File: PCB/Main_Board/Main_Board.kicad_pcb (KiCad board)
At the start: 2 copper layers, 68.2 x 58.9 mm, 57 parts, among them IC1 74LV1T34GVH, J1 USB_B_Micro, J2 Screw_Terminal_01x02, J3 SJ1-3523N, J4 SJ1-3523N, J5 Screw_Terminal_01x04, J6 Screw_Terminal_01x06, Q1 MBT3904DW1, SW1 SW_SPDT, SW2 EN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

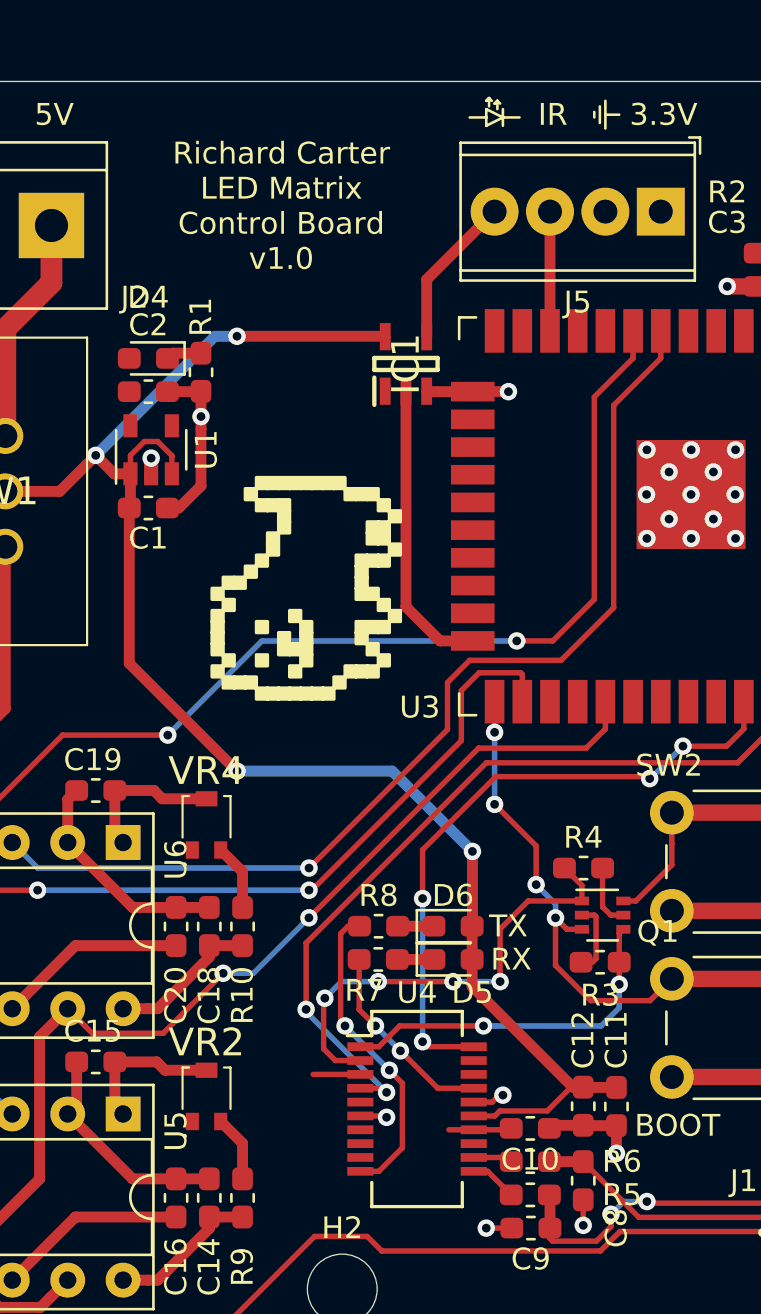
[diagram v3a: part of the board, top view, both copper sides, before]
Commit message: Move references and change renders
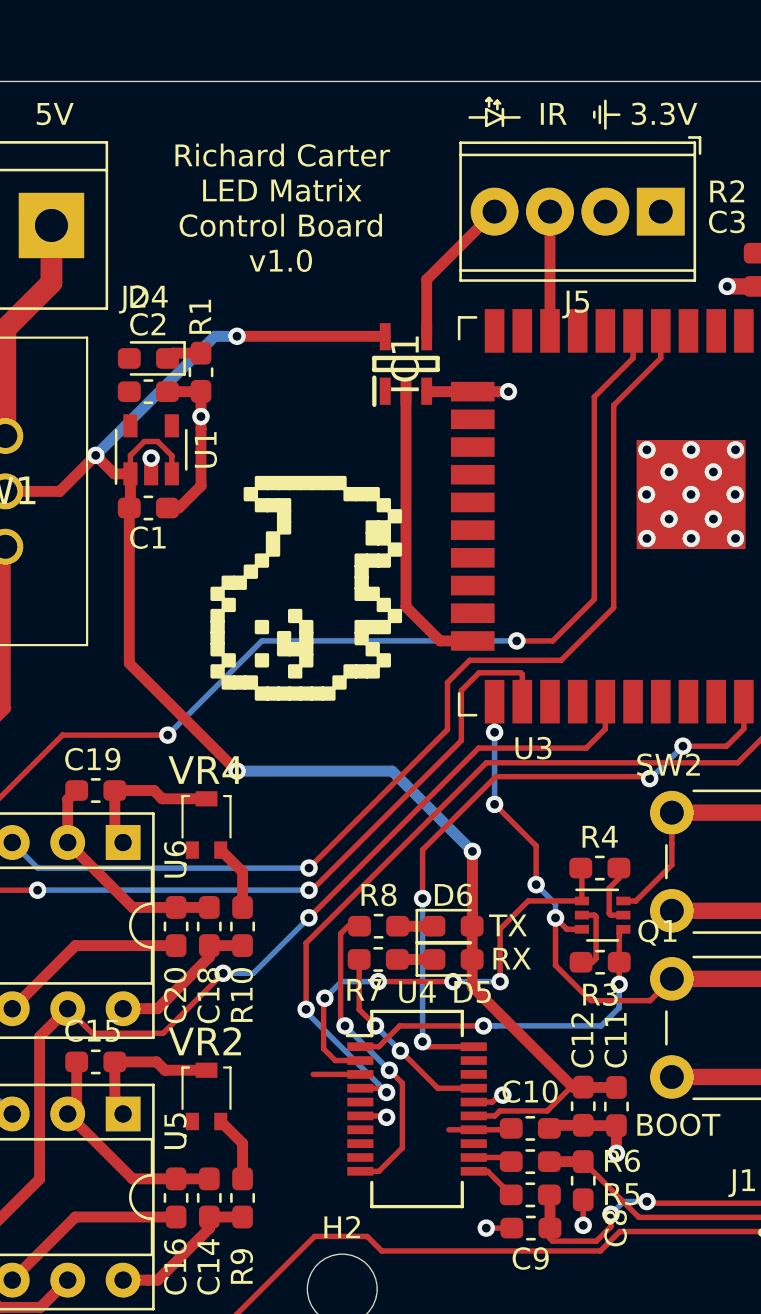
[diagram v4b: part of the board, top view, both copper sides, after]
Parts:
- moved R4 0.75 mm to (70.1, 55.9)
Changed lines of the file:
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@@
     (thickness 1.6)
     (drawings 68)
-    (tracks 420)
+    (tracks 422)
     (zones 0)
     (modules 57)
@@
   )
   (setup
-    (last_trace_width 0.5)
+    (last_trace_width 0.25)
     (user_trace_width 0.5)
     (user_trace_width 0.75)
@@
     (tags "Single 2.4 GHz Wi-Fi and Bluetooth combo  chip")
     (attr smd)
-    (fp_text reference U3 (at 8.763 11.684) (layer F.SilkS)
+    (fp_text reference U3 (at 10.668 6.477) (layer F.SilkS)
       (effects (font (size 1 1) (thickness 0.15)))
     )
@@
   )
   (module Resistor_SMD:R_0603_1608Metric_Pad1.05x0.95mm_HandSolder (layer F.Cu)
-    (at 69.356 55.88 180)
+    (at 70.104 55.88 180)
     (descr "Resistor SMD 0603 (1608 Metric), square (rectangular) end terminal, IPC_7351 nominal with elongated pad for handsoldering. (Body size source: http://www.tortai-tech.com/upload/download/2011102023233369053.pdf), generated with kicad-footprint-generator")
     (tags "resistor handsolder")
@@
     (tags "capacitor handsolder")
     (attr smd)
-    (fp_text reference C10 (at 0 -1.43) (layer F.SilkS)
+    (fp_text reference C10 (at 0 1.651) (layer F.SilkS)
       (effects (font (size 1 1) (thickness 0.15)))
     )
@@
     (arrow2b (pts (xy 24.765 80.391) (xy 25.891504 79.804579)))
   )
-  (gr_text "Richard Carter\nLED Matrix\nControl Board\nv1.0" (at 55.499 25.527) (layer F.SilkS)
+  (gr_text "Richard Carter\nLED Matrix\nControl Board\nv1.0" (at 55.499 25.654) (layer F.SilkS)
     (effects (font (size 1 1) (thickness 0.2)))
   )
@@
   (segment (start 69.931001 58.114001) (end 69.856 58.039) (width 0.25) (layer F.Cu) (net 27))
   (segment (start 70.606 58.039) (end 71.181 58.039) (width 0.25) (layer F.Cu) (net 28))
-  (segment (start 70.231 57.664) (end 70.606 58.039) (width 0.25) (layer F.Cu) (net 28))
-  (segment (start 70.231 55.88) (end 70.231 57.664) (width 0.25) (layer F.Cu) (net 28))
-  (segment (start 69.281 56.68) (end 68.481 55.88) (width 0.25) (layer F.Cu) (net 29))
-  (segment (start 69.281 57.389) (end 69.281 56.68) (width 0.25) (layer F.Cu) (net 29))
+  (segment (start 70.530999 57.963999) (end 70.606 58.039) (width 0.25) (layer F.Cu) (net 28))
+  (segment (start 70.530999 56.803001) (end 70.530999 57.963999) (width 0.25) (layer F.Cu) (net 28))
+  (segment (start 70.979 56.355) (end 70.530999 56.803001) (width 0.25) (layer F.Cu) (net 28))
+  (segment (start 70.979 55.88) (end 70.979 56.355) (width 0.25) (layer F.Cu) (net 28))
   (via (at 65.532 61.087) (size 0.8) (drill 0.4) (layers F.Cu B.Cu) (net 29))
   (segment (start 66.817 57.389) (end 69.281 57.389) (width 0.25) (layer F.Cu) (net 29))
@@
   (segment (start 58.25599 61.087) (end 59.944 61.087) (width 0.25) (layer B.Cu) (net 29))
   (segment (start 57.49399 61.849) (end 58.25599 61.087) (width 0.25) (layer B.Cu) (net 29))
+  (segment (start 69.281 55.932) (end 69.229 55.88) (width 0.25) (layer F.Cu) (net 29))
+  (segment (start 69.281 57.389) (end 69.281 55.932) (width 0.25) (layer F.Cu) (net 29))
   (segment (start 64.9605 69.7865) (end 66.04 70.866) (width 0.25) (layer F.Cu) (net 30))
   (segment (start 64.322 69.7865) (end 64.9605 69.7865) (width 0.25) (layer F.Cu) (net 30))

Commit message: Fix plane routing and change dog icon
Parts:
- U2: footprint Artwork:dog_logo -> Artwork:dog_2_small
- moved U2 5.39 mm to (61.3, 40.4)

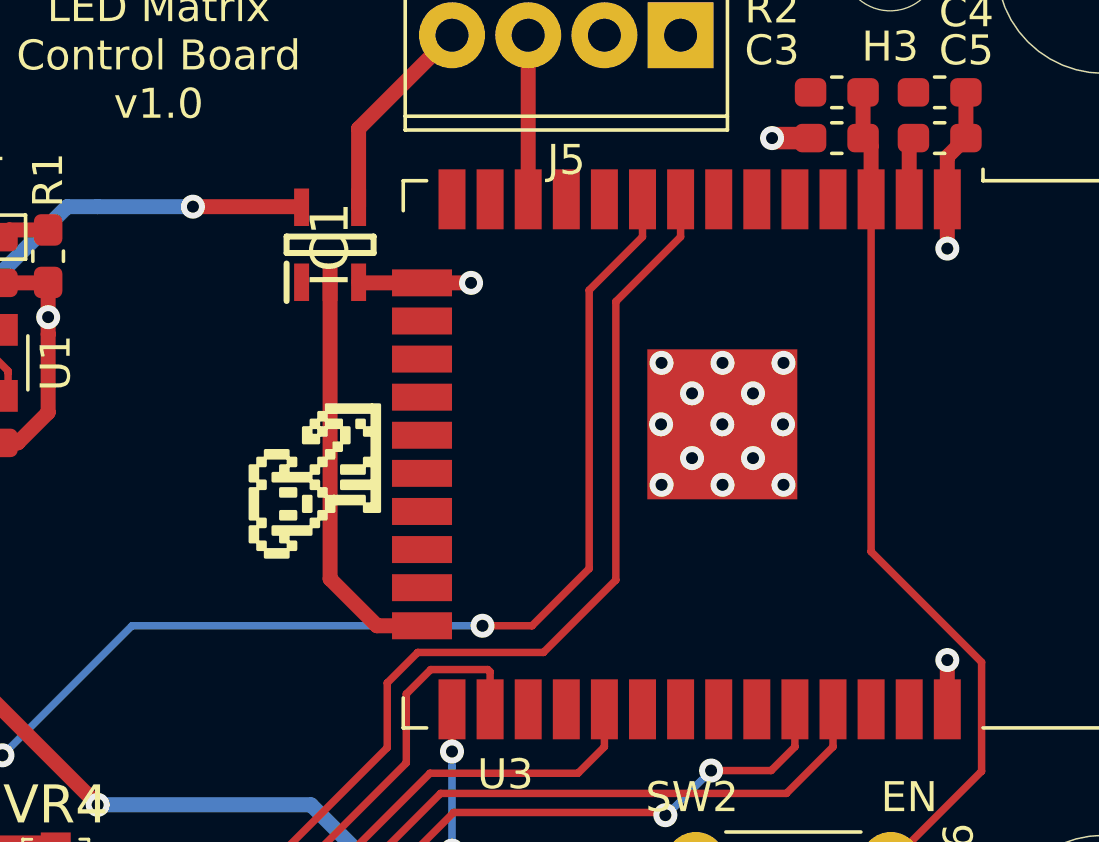
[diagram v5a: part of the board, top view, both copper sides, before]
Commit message: Add new art and JLC order number under ESP32-WROOM-32
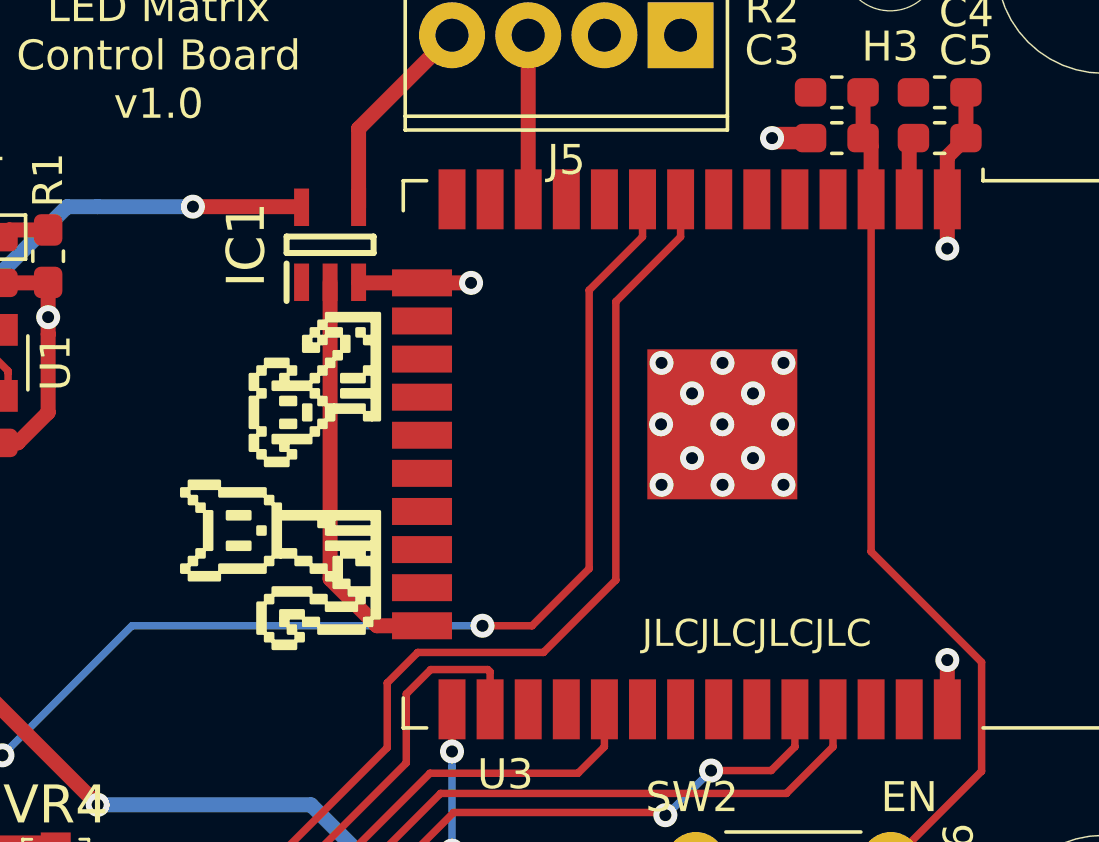
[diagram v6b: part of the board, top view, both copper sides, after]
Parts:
- added ART2: Artwork, Artwork:cat_small_mirrored, F.Cu at (60.6, 43.4)
- moved ART1 3.05 mm to (61.3, 37.3)
- renumbered U2 to ART1
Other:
- board text added: "JLCJLCJLCJLC"
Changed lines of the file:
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@@
   (general
     (thickness 1.6)
-    (drawings 68)
+    (drawings 69)
     (tracks 423)
     (zones 0)
-    (modules 57)
+    (modules 58)
     (nets 84)
   )
@@
     (38 B.Mask user)
     (39 F.Mask user)
-    (40 Dwgs.User user)
+    (40 Dwgs.User user hide)
     (41 Cmts.User user)
     (42 Eco1.User user)
@@
   )
   (setup
-    (last_trace_width 0.5)
+    (last_trace_width 0.25)
     (user_trace_width 0.5)
     (user_trace_width 0.75)
@@
     (add_net "Net-(VR4-Pad1)")
   )
+  (module Artwork:cat_small_mirrored (layer F.Cu)
+    (at 60.579 43.434 90)
+    (fp_text reference ART2 (at 0 -5.334 90) (layer Cmts.User)
+      (effects (font (size 1 1) (thickness 0.15)))
+    )
+    (fp_text value Artwork (at 0.254 3.302 90) (layer F.Fab)
+      (effects (font (size 1 1) (thickness 0.15)))
+    )
+    (fp_poly (pts (xy 2.286 -4.064) (xy 2.54 -4.064) (xy 2.54 -4.318) (xy 2.286 -4.318)) (layer F.SilkS) (width 0.1))
+    (fp_poly (pts (xy 2.032 -3.81) (xy 2.286 -3.81) (xy 2.286 -4.064) (xy 2.032 -4.064)) (layer F.SilkS) (width 0.1))
+    (fp_poly (pts (xy 1.778 -3.556) (xy 2.032 -3.556) (xy 2.032 -3.81) (xy 1.778 -3.81)) (layer F.SilkS) (width 0.1))
+    (fp_poly (pts (xy 2.54 -3.048) (xy 2.794 -3.048) (xy 2.794 -4.064) (xy 2.54 -4.064)) (layer F.SilkS) (width 0.1))
+    (fp_poly (pts (xy 0.508 -3.302) (xy 1.778 -3.302) (xy 1.778 -3.556) (xy 0.508 -3.556)) (layer F.SilkS) (width 0.1))
+    (fp_poly (pts (xy 0.254 -3.556) (xy 0.508 -3.556) (xy 0.508 -3.81) (xy 0.254 -3.81)) (layer F.SilkS) (width 0.1))
+    (fp_poly (pts (xy 0 -3.81) (xy 0.254 -3.81) (xy 0.254 -4.064) (xy 0 -4.064)) (layer F.SilkS) (width 0.1))
+    (fp_poly (pts (xy -0.254 -4.064) (xy 0 -4.064) (xy 0 -4.318) (xy -0.254 -4.318)) (layer F.SilkS) (width 0.1))
+    (fp_poly (pts (xy -0.508 -3.048) (xy -0.254 -3.048) (xy -0.254 -4.064) (xy -0.508 -4.064)) (layer F.SilkS) (width 0.1))
+    (fp_poly (pts (xy 1.524 -2.032) (xy 1.778 -2.032) (xy 1.778 -2.794) (xy 1.524 -2.794)) (layer F.SilkS) (width 0.1))
+    (fp_poly (pts (xy 0.508 -2.032) (xy 0.762 -2.032) (xy 0.762 -2.794) (xy 0.508 -2.794)) (layer F.SilkS) (width 0.1))
+    (fp_poly (pts (xy 2.286 -1.524) (xy 2.54 -1.524) (xy 2.54 -3.048) (xy 2.286 -3.048)) (layer F.SilkS) (width 0.1))
+    (fp_poly (pts (xy -0.254 -1.524) (xy 0 -1.524) (xy 0 -3.048) (xy -0.254 -3.048)) (layer F.SilkS) (width 0.1))
+    (fp_poly (pts (xy 2.032 -1.27) (xy 2.286 -1.27) (xy 2.286 -1.524) (xy 2.032 -1.524)) (layer F.SilkS) (width 0.1))
+    (fp_poly (pts (xy 0 -1.27) (xy 0.254 -1.27) (xy 0.254 -1.524) (xy 0 -1.524)) (layer F.SilkS) (width 0.1))
+    (fp_poly (pts (xy 0.254 -1.016) (xy 2.032 -1.016) (xy 2.032 -1.27) (xy 0.254 -1.27)) (layer F.SilkS) (width 0.1))
+    (fp_poly (pts (xy 0.254 -0.508) (xy 0.508 -0.508) (xy 0.508 -1.016) (xy 0.254 -1.016)) (layer F.SilkS) (width 0.1))
+    (fp_poly (pts (xy 0 0) (xy 0.254 0) (xy 0.254 -0.508) (xy 0 -0.508)) (layer F.SilkS) (width 0.1))
+    (fp_poly (pts (xy -0.254 0.508) (xy 0 0.508) (xy 0 0) (xy -0.254 0)) (layer F.SilkS) (width 0.1))
+    (fp_poly (pts (xy -0.508 0.762) (xy -0.254 0.762) (xy -0.254 0.508) (xy -0.508 0.508)) (layer F.SilkS) (width 0.1))
+    (fp_poly (pts (xy -0.762 1.016) (xy 0.254 1.016) (xy 0.254 0.762) (xy -0.762 0.762)) (layer F.SilkS) (width 0.1))
+    (fp_poly (pts (xy 0.254 1.778) (xy 0.508 1.778) (xy 0.508 1.016) (xy 0.254 1.016)) (layer F.SilkS) (width 0.1))
+    (fp_poly (pts (xy 0 2.032) (xy 0.254 2.032) (xy 0.254 1.524) (xy 0 1.524)) (layer F.SilkS) (width 0.1))
+    (fp_poly (pts (xy 0.508 2.032) (xy 0.762 2.032) (xy 0.762 0.508) (xy 0.508 0.508)) (layer F.SilkS) (width 0.1))
+    (fp_poly (pts (xy -0.762 1.27) (xy -0.508 1.27) (xy -0.508 1.016) (xy -0.762 1.016)) (layer F.SilkS) (width 0.1))
+    (fp_poly (pts (xy -1.016 2.032) (xy -0.762 2.032) (xy -0.762 1.27) (xy -1.016 1.27)) (layer F.SilkS) (width 0.1))
+    (fp_poly (pts (xy -1.27 1.778) (xy -1.016 1.778) (xy -1.016 1.524) (xy -1.27 1.524)) (layer F.SilkS) (width 0.1))
+    (fp_poly (pts (xy -1.524 1.524) (xy -1.27 1.524) (xy -1.27 0.508) (xy -1.524 0.508)) (layer F.SilkS) (width 0.1))
+    (fp_poly (pts (xy -1.27 0.508) (xy -1.016 0.508) (xy -1.016 0) (xy -1.27 0)) (layer F.SilkS) (width 0.1))
+    (fp_poly (pts (xy -2.032 0.254) (xy -1.778 0.254) (xy -1.778 -0.254) (xy -2.032 -0.254)) (layer F.SilkS) (width 0.1))
+    (fp_poly (pts (xy -2.286 1.778) (xy -2.032 1.778) (xy -2.032 0.254) (xy -2.286 0.254)) (layer F.SilkS) (width 0.1))
+    (fp_poly (pts (xy -2.032 2.032) (xy -1.778 2.032) (xy -1.778 1.778) (xy -2.032 1.778)) (layer F.SilkS) (width 0.1))
+    (fp_poly (pts (xy -1.778 -0.254) (xy -1.524 -0.254) (xy -1.524 -1.016) (xy -1.778 -1.016)) (layer F.SilkS) (width 0.1))
+    (fp_poly (pts (xy -2.032 -0.762) (xy -1.778 -0.762) (xy -1.778 -1.016) (xy -2.032 -1.016)) (layer F.SilkS) (width 0.1))
+    (fp_poly (pts (xy -2.286 -0.508) (xy -2.032 -0.508) (xy -2.032 -0.762) (xy -2.286 -0.762)) (layer F.SilkS) (width 0.1))
+    (fp_poly (pts (xy -2.54 -0.254) (xy -2.286 -0.254) (xy -2.286 -0.508) (xy -2.54 -0.508)) (layer F.SilkS) (width 0.1))
+    (fp_poly (pts (xy -2.794 -0.508) (xy -2.54 -0.508) (xy -2.54 -1.27) (xy -2.794 -1.27)) (layer F.SilkS) (width 0.1))
+    (fp_poly (pts (xy -2.54 -1.27) (xy -2.286 -1.27) (xy -2.286 -1.524) (xy -2.54 -1.524)) (layer F.SilkS) (width 0.1))
+    (fp_poly (pts (xy -2.286 -1.524) (xy -1.27 -1.524) (xy -1.27 -1.778) (xy -2.286 -1.778)) (layer F.SilkS) (width 0.1))
+    (fp_poly (pts (xy -1.27 -1.27) (xy -1.016 -1.27) (xy -1.016 -1.524) (xy -1.27 -1.524)) (layer F.SilkS) (width 0.1))
+    (fp_poly (pts (xy -1.016 0) (xy -0.762 0) (xy -0.762 -1.27) (xy -1.016 -1.27)) (layer F.SilkS) (width 0.1))
+    (fp_poly (pts (xy 1.524 2.032) (xy 1.778 2.032) (xy 1.778 -1.016) (xy 1.524 -1.016)) (layer F.SilkS) (width 0.1))
+    (fp_poly (pts (xy 1.016 2.032) (xy 1.27 2.032) (xy 1.27 0.508) (xy 1.016 0.508)) (layer F.SilkS) (width 0.1))
+    (fp_poly (pts (xy 1.27 0.762) (xy 1.524 0.762) (xy 1.524 0.254) (xy 1.27 0.254)) (layer F.SilkS) (width 0.1))
+    (fp_poly (pts (xy -1.778 2.286) (xy 1.778 2.286) (xy 1.778 2.032) (xy -1.778 2.032)) (layer F.SilkS) (width 0.1))
+    (fp_poly (pts (xy 1.016 -1.524) (xy 1.27 -1.524) (xy 1.27 -1.778) (xy 1.016 -1.778)) (layer F.SilkS) (width 0.1))
+  )
   (module Artwork:dog_2_small (layer F.Cu)
-    (at 61.341 40.386 90)
-    (fp_text reference U2 (at 3.556 -2.032 90) (layer Cmts.User)
+    (at 61.341 37.338 90)
+    (fp_text reference ART1 (at 3.556 -2.032 90) (layer Cmts.User)
       (effects (font (size 1 1) (thickness 0.15)))
     )
@@
     (tags "Integrated Circuit")
     (attr smd)
-    (fp_text reference IC1 (at 0 0 90) (layer F.SilkS)
+    (fp_text reference IC1 (at 0 -2.794 90) (layer F.SilkS)
       (effects (font (size 1.27 1.27) (thickness 0.254)))
     )
@@
     )
   )
+  (gr_text JLCJLCJLCJLC (at 75.438 45.72) (layer F.SilkS)
+    (effects (font (size 0.9 0.9) (thickness 0.15)))
+  )
   (gr_line (start 83.439 23.368) (end 83.439 23.495) (layer Edge.Cuts) (width 0.05))
